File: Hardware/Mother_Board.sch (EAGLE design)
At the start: 26 parts, among them IC1 MAX3232CPE, IC2 7805TV, U1 PIC18F26K22-I/SP, U2 25LC1024-E/SM

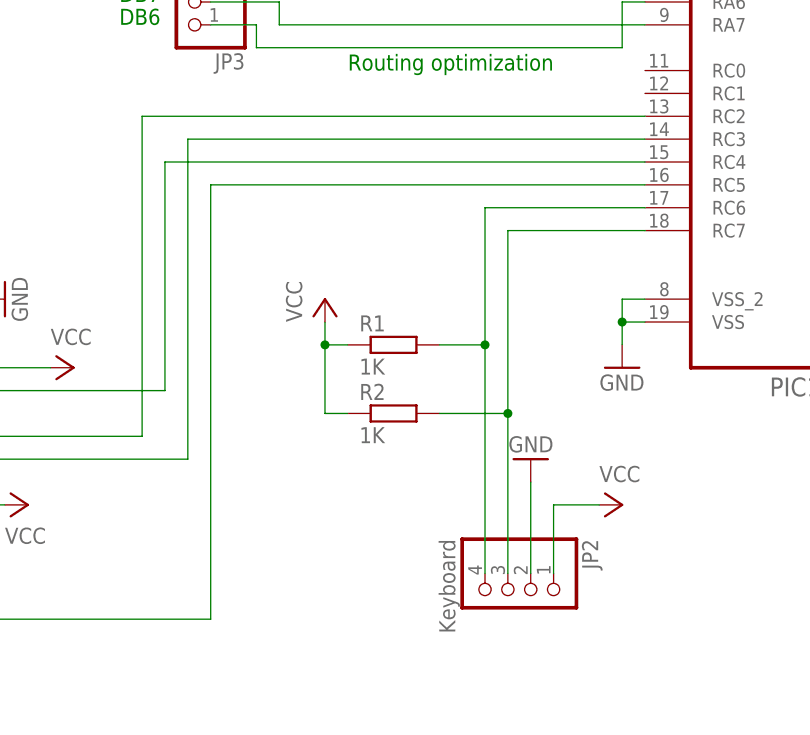
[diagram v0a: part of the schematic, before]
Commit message: Fixed EEPROM SDI and SDO signals routing.
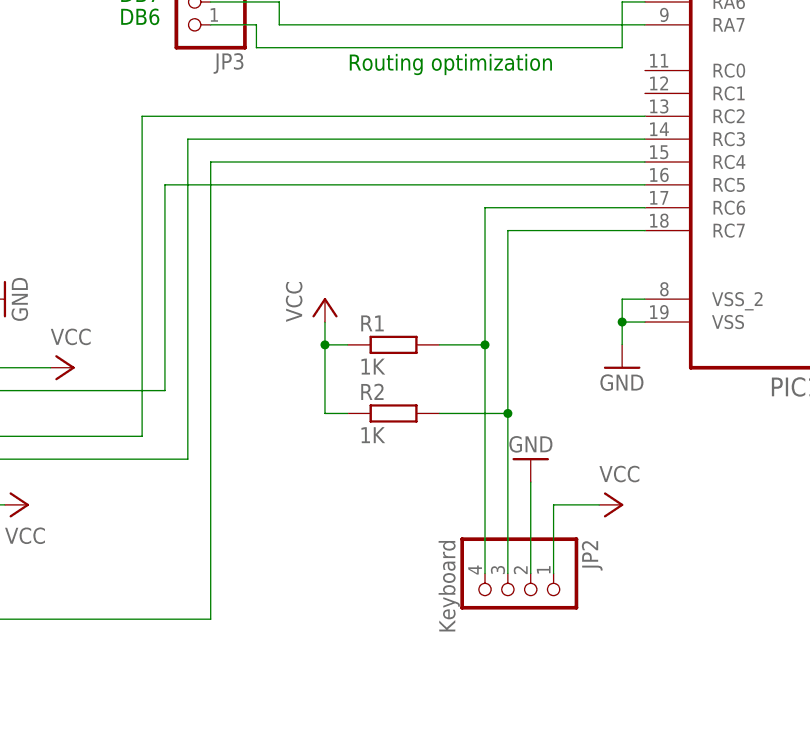
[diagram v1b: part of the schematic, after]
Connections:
- net N$21: now also U1.RC5; no longer U1.RC4
- net N$23: now also U1.RC4; no longer U1.RC5
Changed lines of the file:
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@@
 <pinref part="U2" gate="A" pin="SI"/>
 <wire x1="-38.1" y1="2.54" x2="-15.24" y2="2.54" width="0.1524" layer="91"/>
-<wire x1="-15.24" y1="2.54" x2="-15.24" y2="27.94" width="0.1524" layer="91"/>
-<pinref part="U1" gate="A" pin="RC4"/>
-<wire x1="-15.24" y1="27.94" x2="38.1" y2="27.94" width="0.1524" layer="91"/>
+<wire x1="-15.24" y1="2.54" x2="-15.24" y2="25.4" width="0.1524" layer="91"/>
+<pinref part="U1" gate="A" pin="RC5"/>
+<wire x1="38.1" y1="25.4" x2="-15.24" y2="25.4" width="0.1524" layer="91"/>
 </segment>
 </net>
 <net name="N$23" class="0">
 <segment>
-<pinref part="U1" gate="A" pin="RC5"/>
-<wire x1="38.1" y1="25.4" x2="-10.16" y2="25.4" width="0.1524" layer="91"/>
-<wire x1="-10.16" y1="25.4" x2="-10.16" y2="-22.86" width="0.1524" layer="91"/>
+<wire x1="-10.16" y1="27.94" x2="-10.16" y2="-22.86" width="0.1524" layer="91"/>
 <wire x1="-10.16" y1="-22.86" x2="-76.2" y2="-22.86" width="0.1524" layer="91"/>
 <wire x1="-76.2" y1="-22.86" x2="-76.2" y2="-10.16" width="0.1524" layer="91"/>
 <pinref part="U2" gate="A" pin="SO"/>
 <wire x1="-76.2" y1="-10.16" x2="-73.66" y2="-10.16" width="0.1524" layer="91"/>
+<pinref part="U1" gate="A" pin="RC4"/>
+<wire x1="-10.16" y1="27.94" x2="38.1" y2="27.94" width="0.1524" layer="91"/>
 </segment>
 </net>

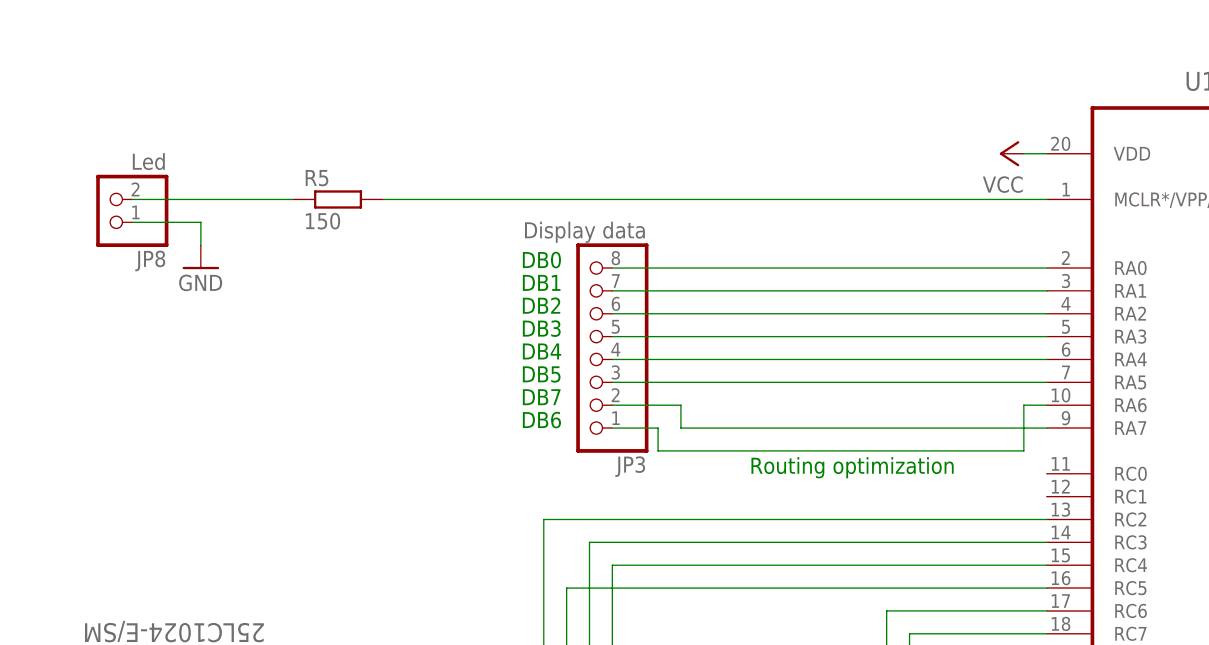
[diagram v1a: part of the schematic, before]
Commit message: Routed led to RC0 instead of RE3 (which is input-only pin).
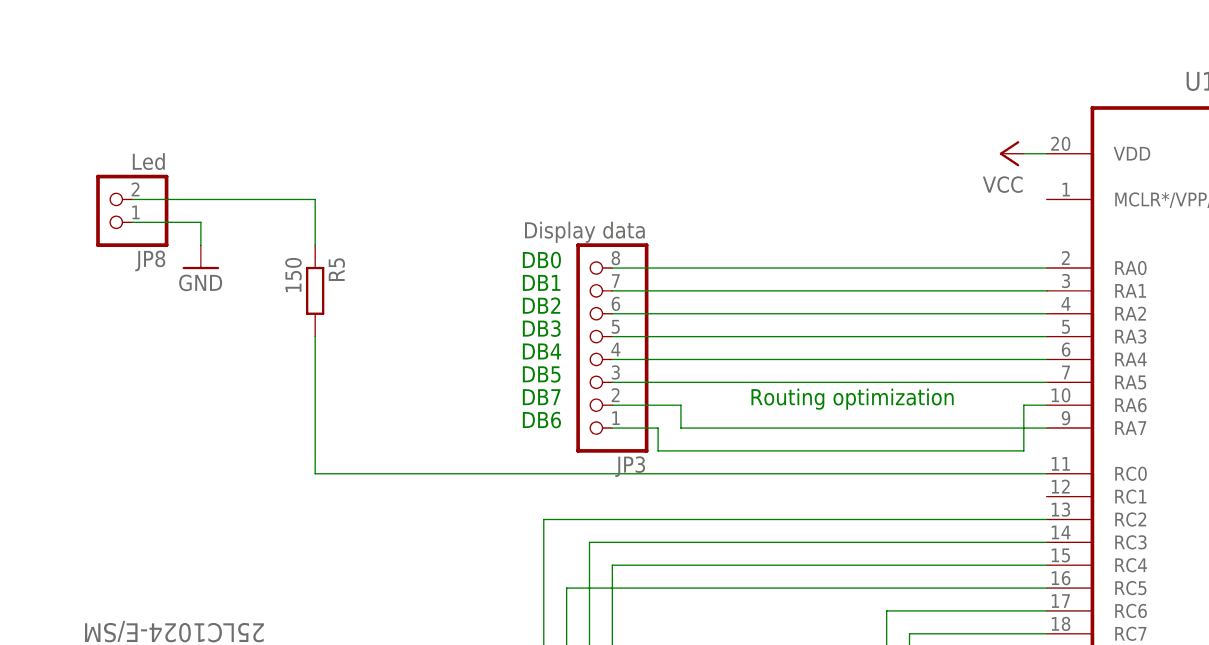
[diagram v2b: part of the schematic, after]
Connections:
- net N$37: now also U1.RC0; no longer U1.MCLR*/VPP/RE3
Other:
- moved on the sheet: R5
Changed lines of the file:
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@@
 <text x="142.24" y="40.64" size="1.778" layer="91">RST</text>
 <text x="-73.66" y="114.3" size="1.778" layer="91">+9V</text>
-<text x="5.08" y="38.1" size="1.778" layer="91">Routing optimization</text>
+<text x="5.08" y="45.72" size="1.778" layer="91">Routing optimization</text>
 </plain>
 <instances>
@@
 <instance part="JP7" gate="G$1" x="-48.26" y="124.46" rot="R90"/>
 <instance part="JP8" gate="G$1" x="-66.04" y="68.58" rot="R180"/>
-<instance part="R5" gate="G$1" x="-40.64" y="68.58"/>
+<instance part="R5" gate="G$1" x="-43.18" y="58.42" rot="R270"/>
 <instance part="GND10" gate="1" x="-55.88" y="60.96"/>
 <instance part="C7" gate="G$1" x="20.32" y="109.22"/>
@@
 </segment>
 </net>
-<net name="N$37" class="0">
-<segment>
-<pinref part="U1" gate="A" pin="MCLR*/VPP/RE3"/>
-<wire x1="38.1" y1="68.58" x2="-35.56" y2="68.58" width="0.1524" layer="91"/>
-<pinref part="R5" gate="G$1" pin="2"/>
-</segment>
-</net>
-<net name="N$38" class="0">
-<segment>
-<pinref part="JP8" gate="G$1" pin="2"/>
-<pinref part="R5" gate="G$1" pin="1"/>
-<wire x1="-63.5" y1="68.58" x2="-45.72" y2="68.58" width="0.1524" layer="91"/>
-</segment>
-</net>
 <net name="N$19" class="0">
 <segment>
@@
 </segment>
 </net>
+<net name="N$37" class="0">
+<segment>
+<pinref part="U1" gate="A" pin="RC0"/>
+<wire x1="38.1" y1="38.1" x2="-43.18" y2="38.1" width="0.1524" layer="91"/>
+<wire x1="-43.18" y1="38.1" x2="-43.18" y2="53.34" width="0.1524" layer="91"/>
+<pinref part="R5" gate="G$1" pin="2"/>
+</segment>
+</net>
+<net name="N$38" class="0">
+<segment>
+<pinref part="JP8" gate="G$1" pin="2"/>
+<pinref part="R5" gate="G$1" pin="1"/>
+<wire x1="-63.5" y1="68.58" x2="-43.18" y2="68.58" width="0.1524" layer="91"/>
+<wire x1="-43.18" y1="68.58" x2="-43.18" y2="63.5" width="0.1524" layer="91"/>
+</segment>
+</net>
